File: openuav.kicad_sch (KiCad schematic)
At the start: 60 parts, among them J1 Conn_01x01, J10 Conn_01x01, J11 Conn_01x01, J12 Conn_01x01, J13 Conn_01x01, J14 Conn_01x01, J15 Conn_01x01, J16 Conn_01x01, J17 Conn_01x01, J18 Conn_01x01, J19 Conn_01x01, J2 Conn_01x01, J20 Conn_01x01, J21 Conn_01x01, J22 Conn_01x01, J23 Conn_01x01, J24 Conn_01x01, J25 Conn_01x01, J26 Conn_01x01, J27 Conn_01x01, J28 Conn_01x01, J29 Conn_01x01, J3 Conn_01x01, J30 Conn_01x01, J31 Conn_01x01, J32 Conn_01x01, J4 Conn_01x01, J5 Conn_01x01, J6 Conn_01x01, J7 Conn_01x01, J8 Conn_01x01, J9 Conn_01x01, J99 USB_C_Receptacle_USB2.0, U1 STM32G431CBUx, U2 AT7456E, U3 LSM6DSR, U4 LPS22HH, U5 L78L33_SOT89, U6 W25N01GVZEIG, U7 TPS5430DDA

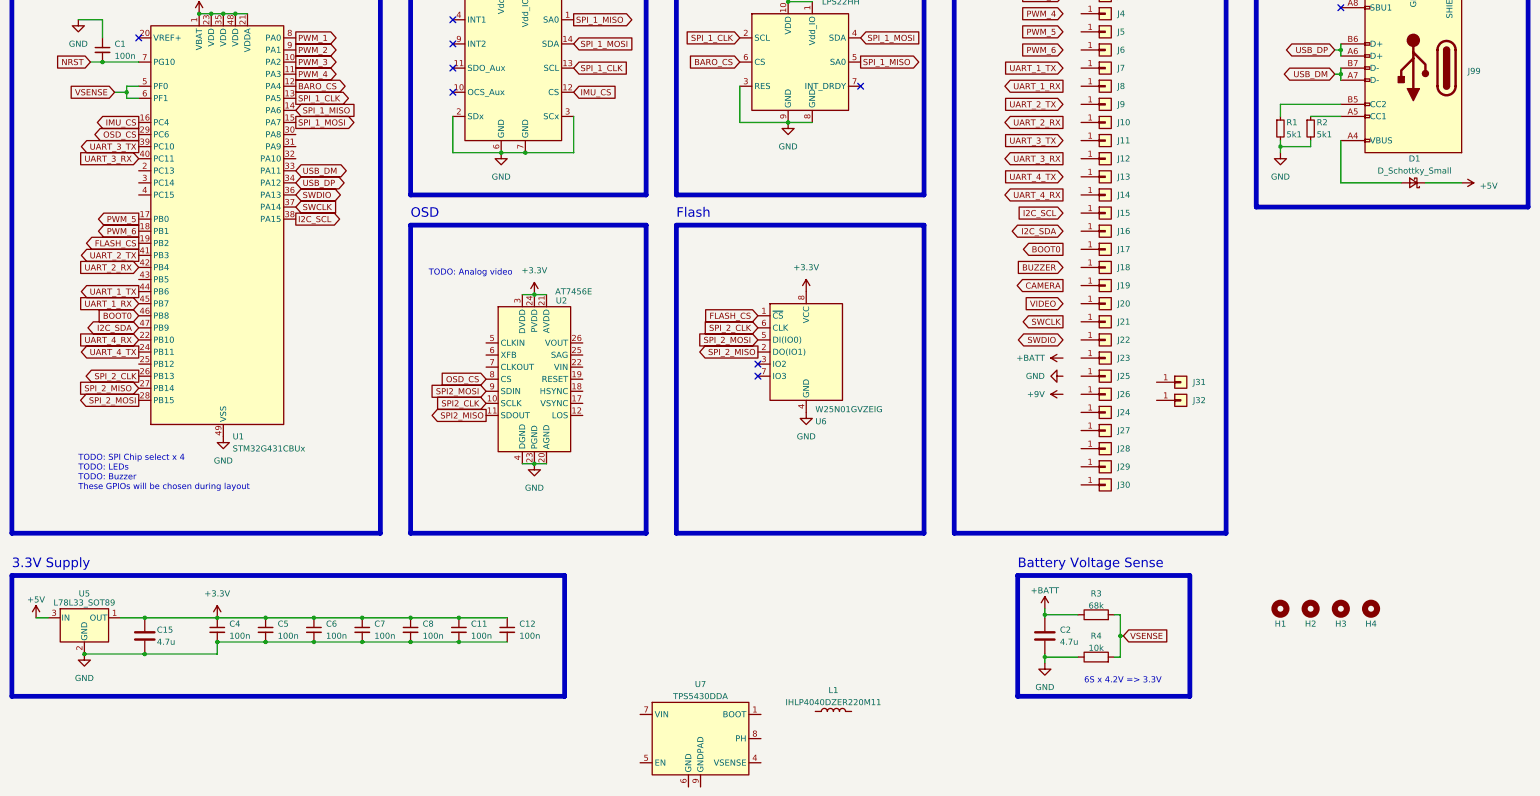
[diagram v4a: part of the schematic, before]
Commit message: remove power supply, start over
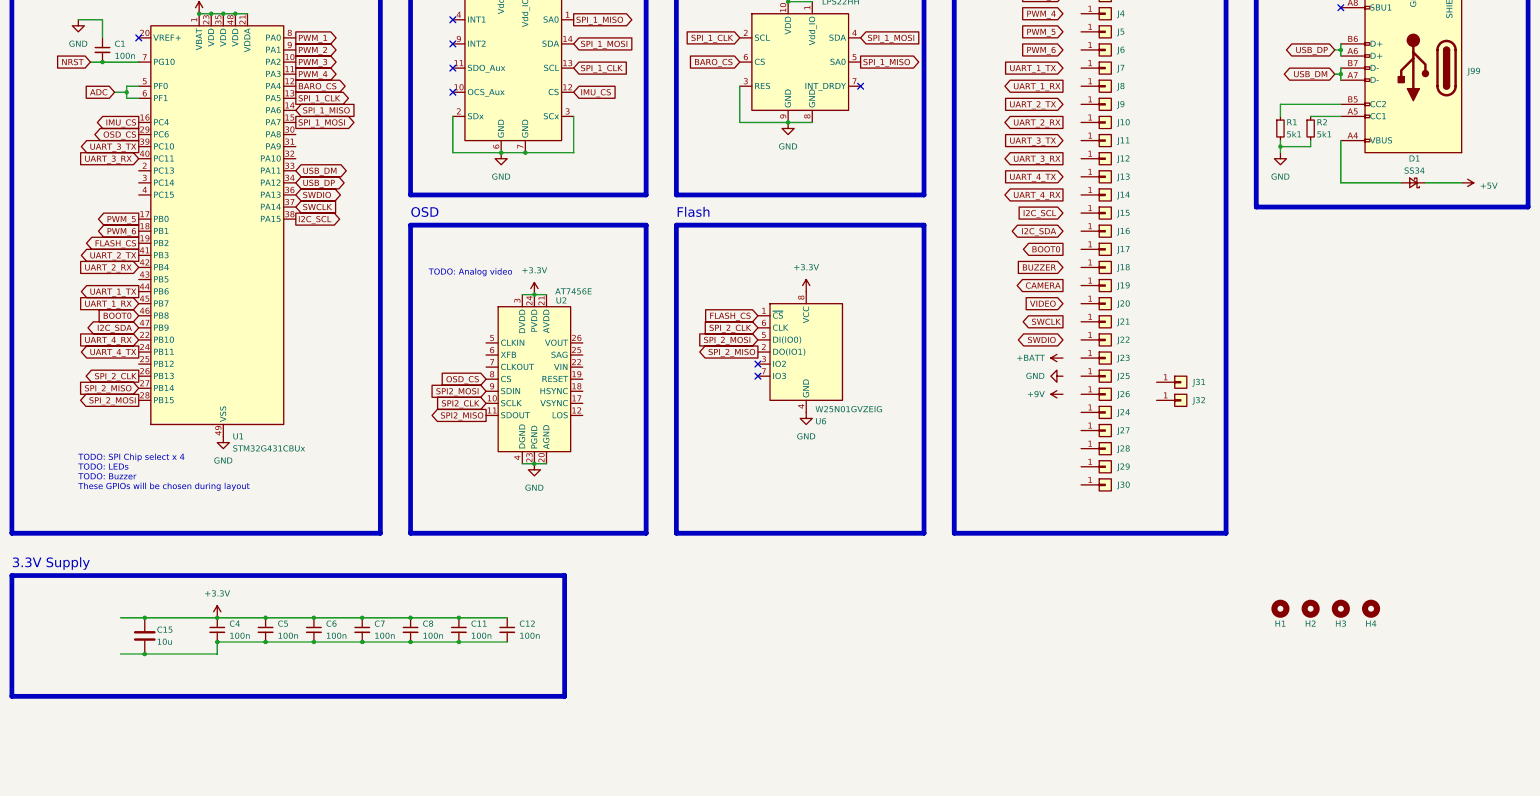
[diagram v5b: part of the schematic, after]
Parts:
- removed C2: 4.7u, Capacitor_SMD:C_0603_1608Metric, symbol Device:C
- removed L1: IHLP4040DZER220M11, Inductor_SMD:L_Vishay_IHLP-4040, symbol Device:L
- removed R3: 68k, Resistor_SMD:R_0402_1005Metric, symbol Device:R
- removed R4: 10k, Resistor_SMD:R_0402_1005Metric, symbol Device:R
- removed U5: L78L33_SOT89, Package_TO_SOT_SMD:SOT-89-3, symbol Regulator_Linear:L78L33_SOT89
- removed U7: TPS5430DDA, Package_SO:TI_SO-PowerPAD-8_ThermalVias, symbol Regulator_Switching:TPS5430DDA
- C15: value 4.7u -> 10u; LCSC C19666 -> (none)
- D1: value D_Schottky_Small -> SS34; footprint (none) -> Diode_SMD:D_SMA; LCSC (none) -> C8678
- U2: LCSC (none) -> C82351
- U6: LCSC (none) -> C88868
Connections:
- net GND: no longer C11.2, C12.2, C15.2, C4.2, C5.2, C6.2, C7.2, C8.2
- net VSENSE renamed ADC
- new net: C11.2, C12.2, C15.2, C4.2, C5.2, C6.2, C7.2, C8.2
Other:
- note removed: "6S x 4.2V => 3.3V"
- note removed: "Battery Voltage Sense"

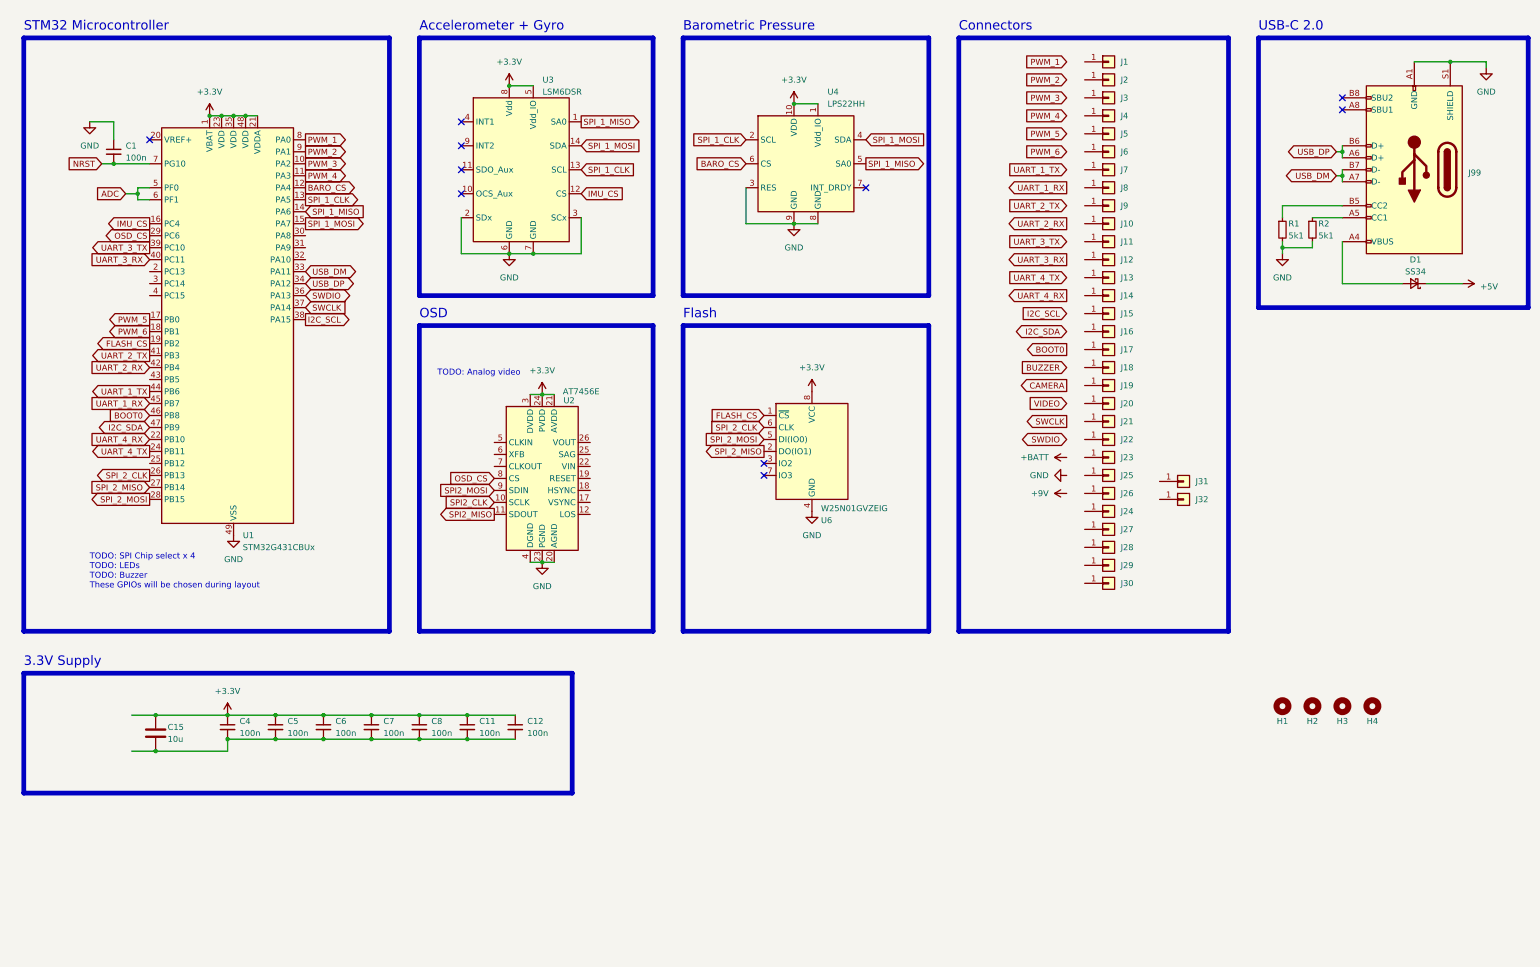
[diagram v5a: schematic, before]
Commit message: Add new 5V SMPS. Rearrange MCU pins to support 3 x SPI
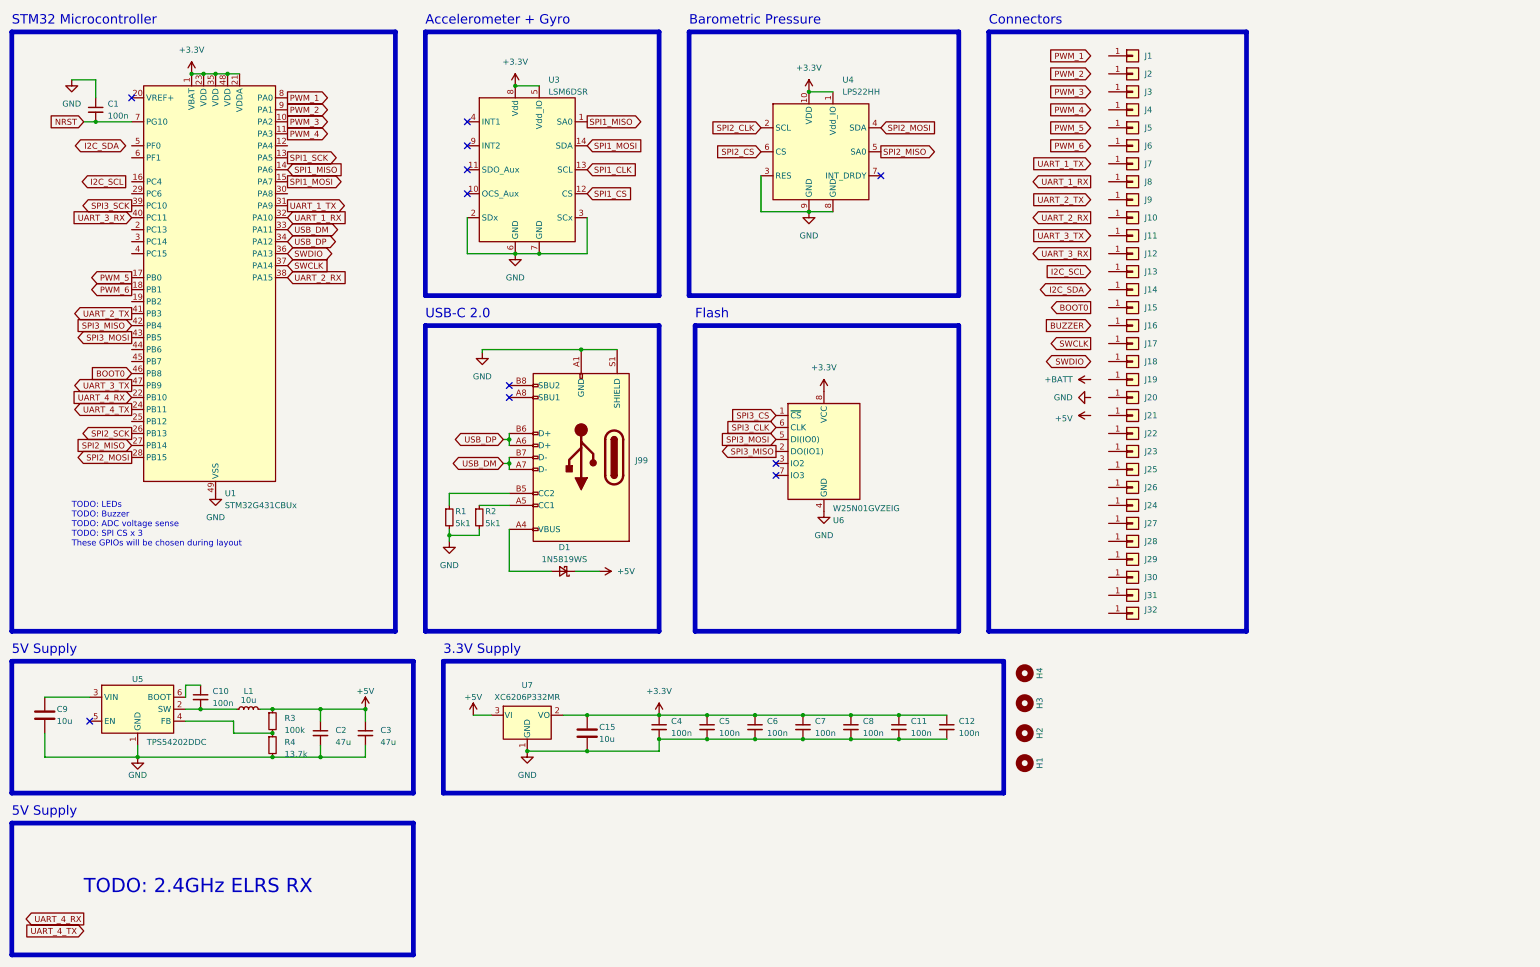
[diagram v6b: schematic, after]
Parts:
- removed U2: AT7456E, Package_SO:TSSOP-28-1EP_4.4x9.7mm_P0.65mm_EP2.85x6.7mm, symbol Max_Video:AT7456E
- added C10: 100n, Capacitor_SMD:C_0402_1005Metric, symbol Device:C_Small
- added C2, C3: 47u, Capacitor_SMD:C_1206_3216Metric, symbol Device:C_Small
- added C9: 10u, Capacitor_SMD:C_1206_3216Metric, symbol Device:C
- added L1: 10u, Inductor_SMD:L_Sunlord_MWSA0603S, symbol Device:L_Small
- added R3: 100k, Resistor_SMD:R_0402_1005Metric, symbol Device:R_Small
- added R4: 13.7k, Resistor_SMD:R_0402_1005Metric, symbol Device:R_Small
- added U5: TPS54202DDC, Package_TO_SOT_SMD:SOT-23-6, symbol Regulator_Switching:TPS54202DDC
- added U7: XC6206P332MR, Package_TO_SOT_SMD:SOT-23-3, symbol Regulator_Linear:XC6206PxxxMR
- D1: value SS34 -> 1N5819WS; footprint Diode_SMD:D_SMA -> Diode_SMD:D_SOD-323; LCSC C8678 -> C191023
- J99: footprint Connector_USB:USB_C_Receptacle_XKB_U262-16XN-4BVC11 -> Connector_USB:USB_C_Receptacle_GCT_USB4105-xx-A_16P_TopMnt_Horizontal
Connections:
- net +3V3: now also U7.2 (VO)
- net +5V: now also C2.1, C3.1, L1.2, R3.1, U7.3 (VI)
- net GND: now also C11.2, C12.2, C15.2, C4.2, C5.2, C6.2, C7.2, C8.2, C2.2, C3.2, C9.2, R4.2, U5.1 (GND), U7.1 (GND)
- net I2C_SCL: no longer U1.38 (PA15)
- net I2C_SDA: no longer U1.47 (PB9)
- net SPI2_CLK: now also U4.2 (SCL)
- net SPI2_MISO: now also U1.27 (PB14), U4.5 (SA0)
- net SPI2_MOSI: now also U1.28 (PB15), U4.4 (SDA)
- net UART_1_RX: now also U1.32 (PA10); no longer U1.45 (PB7)
- net UART_1_TX: now also U1.31 (PA9); no longer U1.44 (PB6)
- net UART_2_RX: now also U1.38 (PA15); no longer U1.42 (PB4)
- net UART_3_TX: now also U1.47 (PB9); no longer U1.39 (PC10)
- net SPI3_MOSI: now reaches U1.43 (PB5)
- net SPI3_MOSI: now also U6.5 (DI(IO0))
- net ADC: no longer names the net of U1.5 (PF0)
- net ADC: no longer U1.6 (PF1)
- net BARO_CS: no longer names the net of U1.12 (PA4)
- net BARO_CS: no longer U4.6 (CS)
- net FLASH_CS: no longer names the net of U1.19 (PB2)
- net FLASH_CS: no longer U6.1 (~{CS})
- net IMU_CS: no longer names the net of U1.16 (PC4)
- net IMU_CS: no longer U3.12 (CS)
- net OSD_CS: no longer names the net of U1.29 (PC6)
- removed net SPI_1_CLK: U1.13 (PA5), U3.13 (SCL), U4.2 (SCL)
- net SPI_1_MISO renamed SPI1_MISO
- net SPI1_MISO: no longer U4.5 (SA0)
- net SPI_1_MOSI renamed SPI1_MOSI
- net SPI1_MOSI: no longer U4.4 (SDA)
- net SPI_2_CLK renamed SPI2_SCK
- net SPI2_SCK: no longer U6.6 (CLK)
- net SPI_2_MISO renamed SPI3_MISO
- net SPI3_MISO: now also U1.42 (PB4); no longer U1.27 (PB14)
- removed net SPI_2_MOSI: U1.28 (PB15), U6.5 (DI(IO0))
- new net: C10.1, U5.6 (BOOT)
- new net: C10.2, L1.1, U5.2 (SW)
- new net: C9.1, U5.3 (VIN)
- new net: R3.2, R4.1, U5.4 (FB)
- new net SPI1_CLK: U3.13 (SCL)
- new net SPI1_CS: U3.12 (CS)
- new net SPI1_SCK: U1.13 (PA5)
- new net SPI2_CS: U4.6 (CS)
- new net SPI3_CLK: U6.6 (CLK)
- new net SPI3_CS: U6.1 (~{CS})
- new net SPI3_SCK: U1.39 (PC10)
- no-connect marks 10 -> 11
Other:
- note added: "5V Supply"
- note added: "TODO: 2.4GHz ELRS RX"
- note added: "TODO: LEDs TODO: Buzzer TODO: ADC voltage sense TODO: SPI CS x 3 These GPIOs will be chosen during layout"
- note removed: "OSD"
- note removed: "TODO: Analog video"
- note removed: "TODO: SPI Chip select x 4 TODO: LEDs TODO: Buzzer These GPIOs will be chosen during layout"
- moved on the sheet: C1, C11, C12, C15, C4, C5, C6, C7, C8, D1, H1, H2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
